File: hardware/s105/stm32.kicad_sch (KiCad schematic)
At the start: 48 parts

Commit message: разместила схожие блоки
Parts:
- removed C? (x2): 100nF, Capacitor_SMD:C_0603_1608Metric, symbol Device:C
- removed C?: 22uF, Capacitor_SMD:C_0603_1608Metric, symbol Device:C
- removed C?: 1uF, Capacitor_SMD:C_0603_1608Metric, symbol Device:C
- removed C? (x2): 6.8pF, Capacitor_SMD:C_0603_1608Metric, symbol Device:C
- removed D?: B5819W, Diode_SMD:D_SOD-123, symbol Device:D_Schottky
- removed D?: LED-GREEN, LED_SMD:LED_0805_2012Metric, symbol Device:LED
- removed D?: LED-RED, LED_SMD:LED_0603_1608Metric, symbol Device:LED
- removed D?: SRV05-4, Package_TO_SOT_SMD:SOT-23-6, symbol Power_Protection:NUP4202
- removed D?: BAV70, Package_TO_SOT_SMD:SOT-23, symbol Diode:BAV70
- removed FB?: FILTER, Resistor_SMD:R_0603_1608Metric_Pad1.05x0.95mm_HandSolder, symbol Device:Ferrite_Bead
- removed FID? (x2): Fiducial, Fiducial:Fiducial_0.5mm_Mask1mm, symbol Mechanical:Fiducial
- removed J?: TC2030, Connector:Tag-Connect_TC2030-IDC-NL_2x03_P1.27mm_Vertical, symbol Connector:Conn_01x06_Male
- removed J?: Conn_02x05_Odd_Even, Connector_PinSocket_2.54mm:PinSocket_2x05_P2.54mm_Vertical_SMD, symbol Connector_Generic:Conn_02x05_Odd_Even
- removed J?: USB_B_Mini, hellen-one-common:USB-MINI-B-VERTICAL, symbol hellen-one-common:USB_B_Mini
- removed R?: 2.2k, Resistor_SMD:R_0603_1608Metric, symbol Device:R
- removed R?: 1k, Resistor_SMD:R_0603_1608Metric, symbol Device:R
- removed R?: 100K, Resistor_SMD:R_0603_1608Metric, symbol Device:R
- removed SW? (x2): SW_Push, Button_Switch_SMD:SW_SPST_CK_RS282G05A3, symbol Switch:SW_Push
- removed SW? (x2): SW_Push, Button_Switch_SMD:SW_Push_SPST_NO_Alps_SKRK, symbol Switch:SW_Push
- removed U?: LM1117-3.3, Package_TO_SOT_SMD:SOT-223-3_TabPin2, symbol Regulator_Linear:LM1117-3.3
- removed U? (x2): molex_48pin_MRE, symbol rusefi_Molex_MRE_Connector:molex_48pin_MRE
- removed Y?: 32768 Hz, Crystal:Crystal_SMD_3215-2Pin_3.2x1.5mm, symbol Device:Crystal_Small
- added C52, C53: 100nF, Capacitor_SMD:C_0603_1608Metric, symbol Device:C
- added R201: R0603, Resistor_SMD:R_0603_1608Metric, symbol Device:R
- added R202: 300, Resistor_SMD:R_0603_1608Metric, symbol Device:R
- J1: renamed from J?; footprint Connector_JST:JST_EH_B5B-EH-A_1x05_P2.50mm_Vertical -> Connector_JST:JST_EH_B6B-EH-A_1x06_P2.50mm_Vertical; symbol Connector_Generic:Conn_01x05 -> Connector_Generic:Conn_01x06
- gave numbers to parts that had none: 19
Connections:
- net VDDA is gone; now on net VDD: C12.2, C13.2, C8.2, C9.2, U2.21 (VREF+), U2.22 (VDDA)
- net 5V: now also J1.5 (Pin_5)
- net GND: now also J1.2 (Pin_2), C52.1, C53.1, R201.2; no longer J1.5 (Pin_5)
- net PA0: now also C53.2
- net PA1: now also C52.2
- net PA10: no longer J1.1 (Pin_1)
- net PA13: now also J1.1 (Pin_1)
- net PA14: now also J1.3 (Pin_3)
- net PC1: now also R201.1
- net VDD: now also J1.4 (Pin_4)
- net at C7.1, X1.1: now also R202.1; no longer U2.13 (PH1)
- net USB_D+ renamed PA12
- net PA12: no longer J1.3 (Pin_3)
- net USB_D- renamed PA11
- net PA11: no longer J1.2 (Pin_2)
- net USB_VBUS renamed PA9
- net PA9: no longer J1.4 (Pin_4)
- net Vrtcc: no longer names the net of U2.6 (VBAT)
- new net: R202.2, U2.13 (PH1)
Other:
- note removed: "3.3v"
- note removed: "SWD"
- note removed: "USB ESD protection"
- note removed: "USB bulk head connector USB UB-20PMFP-LC7002 Cover / Cap CAP-WADMLP_ _"
- note removed: "USB power"

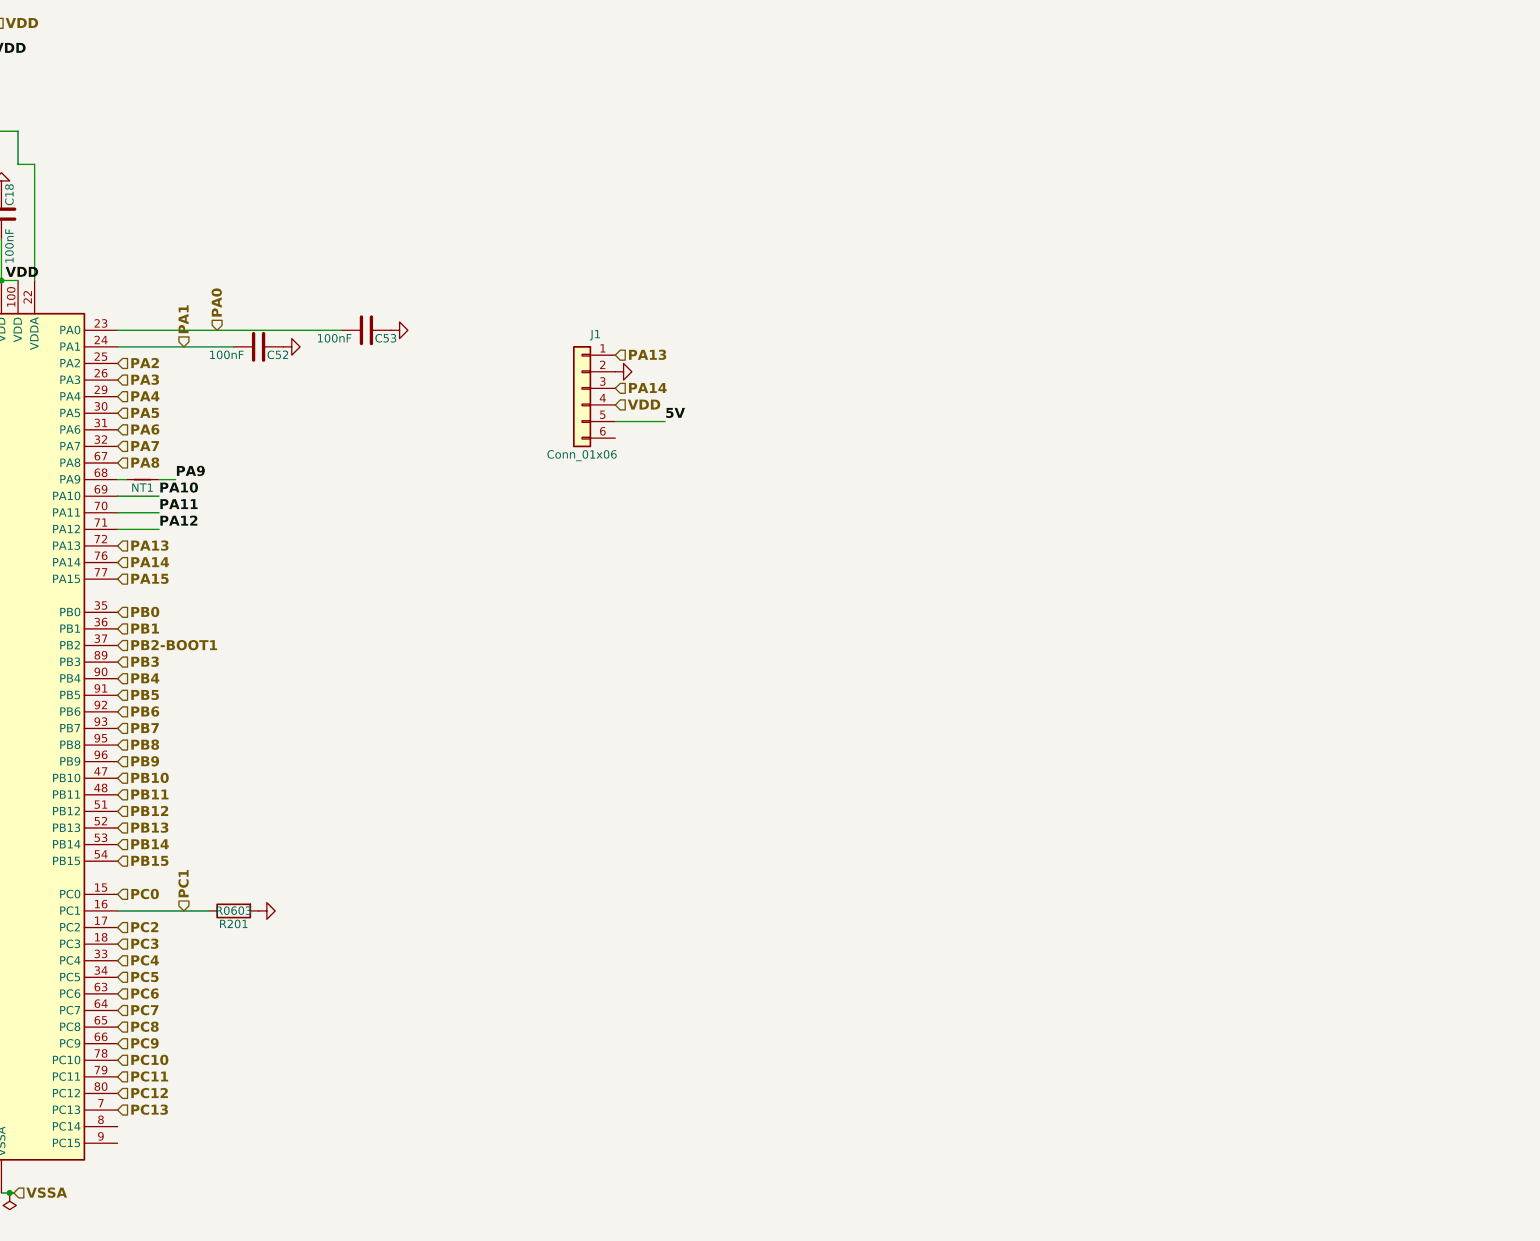
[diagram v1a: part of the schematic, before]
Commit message: вписала в габариты платы, продолжила опознание
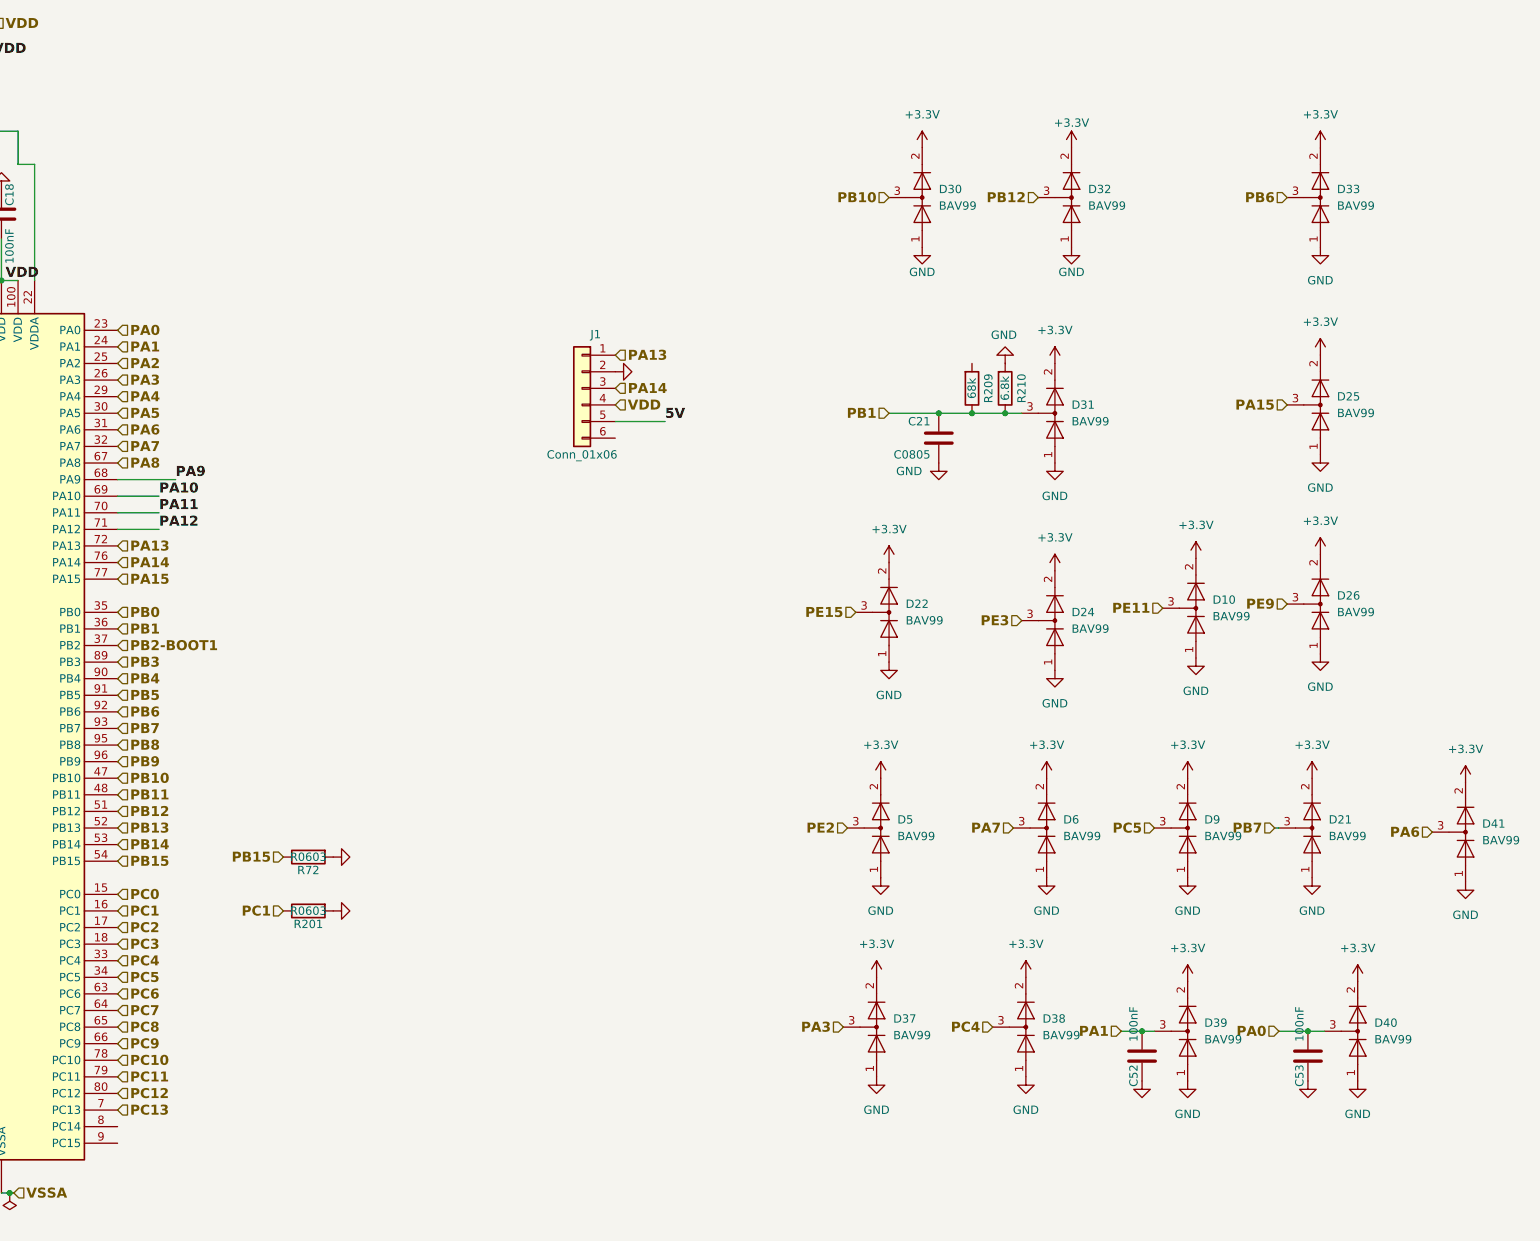
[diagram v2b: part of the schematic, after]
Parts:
- removed NT1: Net-Tie_2, rusEFI_Ola:Net-Tie_2_8.5mil, symbol Device:Net-Tie_2
- added C21: C0805, Capacitor_SMD:C_0805_2012Metric, symbol Device:C
- added D10, D21, D22, D24, D25, D26, D30, D31, D32, D33, D37, D38, D39, D40, D41, D5, D6, D9: BAV99, Package_TO_SOT_SMD:SOT-23, symbol Diode:BAV99
- added R209: 68k, Resistor_SMD:R_0603_1608Metric, symbol Device:R
- added R210: 6.8k, Resistor_SMD:R_0603_1608Metric, symbol Device:R
- added R72: R0603, Resistor_SMD:R_0603_1608Metric, symbol Device:R
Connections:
- net GND: now also C21.2, D10.1 (K), D21.1 (K), D22.1 (K), D24.1 (K), D25.1 (K), D26.1 (K), D30.1 (K), D31.1 (K), D32.1 (K), D33.1 (K), D37.1 (K), D38.1 (K), D39.1 (K), D40.1 (K), D41.1 (K), D5.1 (K), D6.1 (K), D9.1 (K), R210.2, R72.2
- net PA0: now also D40.3 (K)
- net PA1: now also D39.3 (K)
- net PA15: now also D25.3 (K)
- net PA3: now also D37.3 (K)
- net PA6: now also D41.3 (K)
- net PA7: now also D6.3 (K)
- net PA9: now also U2.68 (PA9)
- net PB1: now also C21.1, D31.3 (K), R209.1, R210.1
- net PB10: now also D30.3 (K)
- net PB12: now also D32.3 (K)
- net PB15: now also R72.1
- net PB6: now also D33.3 (K)
- net PB7: now also D21.3 (K)
- net PC4: now also D38.3 (K)
- net PC5: now also D9.3 (K)
- net PE11: now also D10.3 (K)
- net PE15: now also D22.3 (K)
- net PE2: now also D5.3 (K)
- net PE3: now also D24.3 (K)
- net PE9: now also D26.3 (K)
- new net +3.3V: D10.2 (A), D21.2 (A), D22.2 (A), D24.2 (A), D25.2 (A), D26.2 (A), D30.2 (A), D31.2 (A), D32.2 (A), D33.2 (A), D37.2 (A), D38.2 (A), D39.2 (A), D40.2 (A), D41.2 (A), D5.2 (A), D6.2 (A), D9.2 (A)
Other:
- moved on the sheet: C52, C53, R201

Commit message: новые модули, продолжение расположения
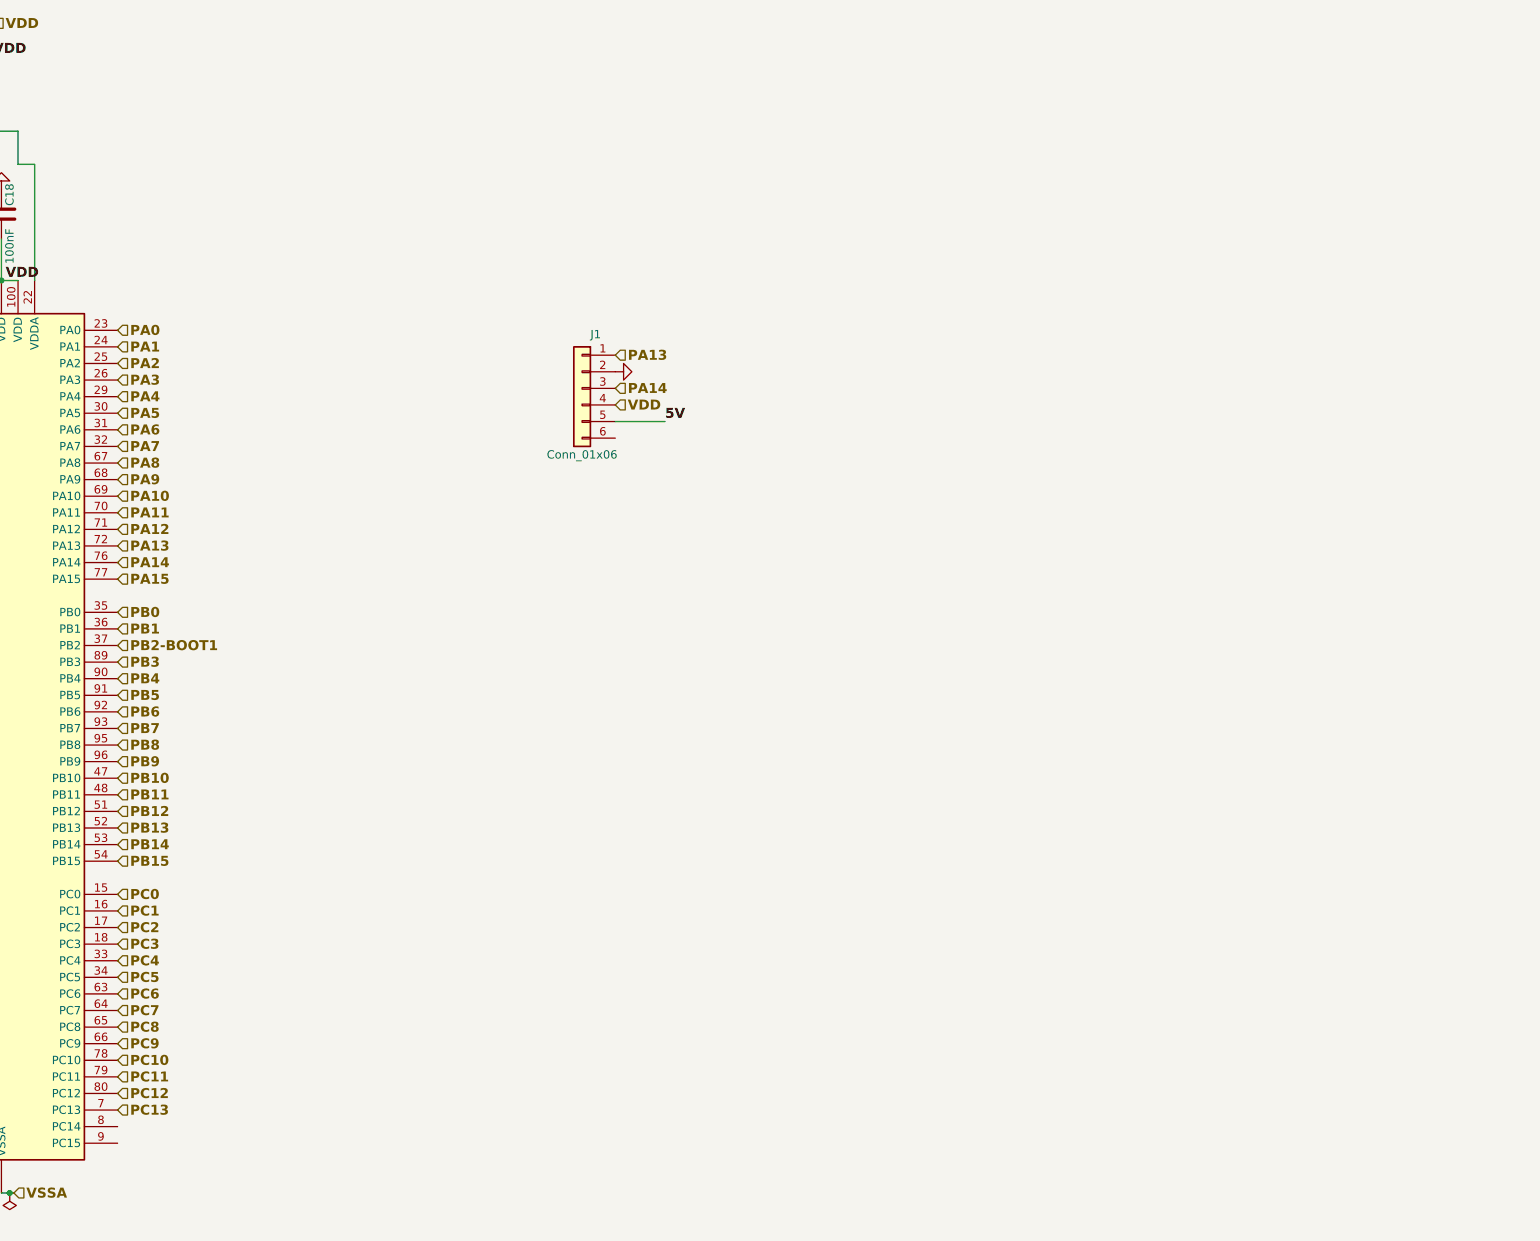
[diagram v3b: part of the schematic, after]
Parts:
- removed C21: C0805, Capacitor_SMD:C_0805_2012Metric, symbol Device:C
- removed C52, C53: 100nF, Capacitor_SMD:C_0603_1608Metric, symbol Device:C
- removed D10, D21, D22, D24, D25, D26, D30, D31, D32, D33, D37, D38, D39, D40, D41, D5, D6, D9: BAV99, Package_TO_SOT_SMD:SOT-23, symbol Diode:BAV99
- removed R201, R72: R0603, Resistor_SMD:R_0603_1608Metric, symbol Device:R
- removed R209: 68k, Resistor_SMD:R_0603_1608Metric, symbol Device:R
- removed R210: 6.8k, Resistor_SMD:R_0603_1608Metric, symbol Device:R

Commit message: заполняем плату дальше
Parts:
- added R254: 4.7k, Resistor_SMD:R_0603_1608Metric, symbol Device:R
- added R255: NM, Resistor_SMD:R_0603_1608Metric, symbol Device:R
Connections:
- net 5V: now also R254.1
- net GND: now also R255.2
- net PB2-BOOT1: now also R254.2, R255.1
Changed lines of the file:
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@@
   (junction (at 120.65 67.945) (diameter 0) (color 0 0 0 0)
   )
+  (junction (at 207.01 146.05) (diameter 0) (color 0 0 0 0)
+  )
   (junction (at 152.4 63.5) (diameter 0) (color 0 0 0 0)
   )
@@
     (stroke (width 0) (type default) (color 0 0 0 0))
   )
+  (wire (pts (xy 217.17 146.05) (xy 207.01 146.05))
+    (stroke (width 0) (type default) (color 0 0 0 0))
+  )
   (wire (pts (xy 156.21 88.9) (xy 156.21 90.17))
     (stroke (width 0) (type default) (color 0 0 0 0))
@@
     (stroke (width 0) (type default) (color 0 0 0 0))
   )
+  (wire (pts (xy 207.01 146.05) (xy 186.69 146.05))
+    (stroke (width 0) (type default) (color 0 0 0 0))
+  )
   (wire (pts (xy 123.19 138.43) (xy 123.19 142.24))
     (stroke (width 0) (type default) (color 0 0 0 0))
@@
   )
   (wire (pts (xy 129.54 142.24) (xy 123.19 142.24))
-    (stroke (width 0) (type default) (color 0 0 0 0))
-  )
-  (wire (pts (xy 270.51 111.76) (xy 262.89 111.76))
     (stroke (width 0) (type default) (color 0 0 0 0))
   )
@@
     (effects (font (size 1.524 1.524) (thickness 0.3048) bold) (justify left bottom))
   )
+  (label "5V" (at 207.01 138.43 0)
+    (effects (font (size 1.524 1.524) (thickness 0.3048) bold) (justify left bottom))
+  )
   (label "VREF" (at 105.41 67.945 0)
     (effects (font (size 1.27 1.27)) (justify left bottom))
@@
     (effects (font (size 1.27 1.27)) (justify left bottom))
   )
-  (label "5V" (at 270.51 111.76 0)
-    (effects (font (size 1.524 1.524) (thickness 0.3048) bold) (justify left bottom))
-  )
   (label "VDD" (at 96.52 97.79 180)
     (effects (font (size 1.524 1.524) (thickness 0.3048) bold) (justify right bottom))
@@
     (effects (font (size 1.524 1.524) (thickness 0.3048) bold) (justify right))
   )
+  (hierarchical_label "5V" (shape input) (at 262.89 111.76 0)
+    (effects (font (size 1.524 1.524) (thickness 0.3048) bold) (justify left))
+  )
   (hierarchical_label "PD2" (shape input) (at 140.97 189.23 180)
     (effects (font (size 1.524 1.524) (thickness 0.3048) bold) (justify right))
@@
     (effects (font (size 1.524 1.524) (thickness 0.3048) bold) (justify right))
   )
-  (hierarchical_label "PB2-BOOT1" (shape input) (at 186.69 146.05 0)
+  (hierarchical_label "PB2-BOOT1" (shape input) (at 217.17 146.05 0)
     (effects (font (size 1.524 1.524) (thickness 0.3048) bold) (justify left))
   )
@@
       (effects (font (size 1.27 1.27)) hide)
     )
+    (pin "1")
+    (pin "2")
+  )
+  (symbol (lib_id "Device:R") (at 207.01 142.24 0) (mirror y) (unit 1)
+    (in_bom yes) (on_board yes)
+    (property "Reference" "R254" (id 0) (at 210.82 142.875 0))
+    (property "Value" "4.7k" (id 1) (at 211.455 140.97 0))
+    (property "Footprint" "Resistor_SMD:R_0603_1608Metric" (id 2) (at 208.788 142.24 90)
+      (effects (font (size 1.27 1.27)) hide)
+    )
+    (property "Datasheet" "~" (id 3) (at 207.01 142.24 0)
+      (effects (font (size 1.27 1.27)) hide)
+    )
+    (pin "1")
+    (pin "2")
+  )
+  (symbol (lib_id "power:GND") (at 207.01 153.67 0) (unit 1)
+    (in_bom yes) (on_board yes)
+    (property "Reference" "#PWR0348" (id 0) (at 207.01 153.67 0)
+      (effects (font (size 0.762 0.762)) hide)
+    )
+    (property "Value" "GND" (id 1) (at 207.01 155.448 0)
+      (effects (font (size 0.762 0.762)) hide)
+    )
+    (property "Footprint" "" (id 2) (at 207.01 153.67 0)
+      (effects (font (size 1.524 1.524)) hide)
+    )
+    (property "Datasheet" "" (id 3) (at 207.01 153.67 0)
+      (effects (font (size 1.524 1.524)) hide)
+    )
+    (pin "1")
+  )
+  (symbol (lib_id "Device:R") (at 207.01 149.86 0) (mirror y) (unit 1)
+    (in_bom yes) (on_board yes)
+    (property "Reference" "R255" (id 0) (at 209.55 147.955 0))
+    (property "Value" "NM" (id 1) (at 209.55 149.86 0))
+    (property "Footprint" "Resistor_SMD:R_0603_1608Metric" (id 2) (at 208.788 149.86 90)
+      (effects (font (size 1.27 1.27)) hide)
+    )
+    (property "Datasheet" "~" (id 3) (at 207.01 149.86 0)
+      (effects (font (size 1.27 1.27)) hide)
+    )

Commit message: +knock
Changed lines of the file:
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@@
+    (stroke (width 0) (type default) (color 0 0 0 0))
+  )
+  (wire (pts (xy 270.51 111.76) (xy 262.89 111.76))
     (stroke (width 0) (type default) (color 0 0 0 0))
   )
@@
     (effects (font (size 1.27 1.27)) (justify left bottom))
   )
+  (label "5V" (at 270.51 111.76 0)
+    (effects (font (size 1.524 1.524) (thickness 0.3048) bold) (justify left bottom))
+  )
   (label "VDD" (at 96.52 97.79 180)
     (effects (font (size 1.524 1.524) (thickness 0.3048) bold) (justify right bottom))
@@
     (effects (font (size 1.524 1.524) (thickness 0.3048) bold) (justify right))
   )
-  (hierarchical_label "5V" (shape input) (at 262.89 111.76 0)
-    (effects (font (size 1.524 1.524) (thickness 0.3048) bold) (justify left))
-  )
   (hierarchical_label "PD2" (shape input) (at 140.97 189.23 180)
